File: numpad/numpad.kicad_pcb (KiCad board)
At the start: 2 copper layers, 81.3 x 121.9 mm, 50 parts, among them J1 USB_mini_micro_B, K1 KEYSW, K10 KEYSW, K11 KEYSW, K12 KEYSW, K13 KEYSW, K14 KEYSW, K15 KEYSW, K16 KEYSW, K17 KEYSW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

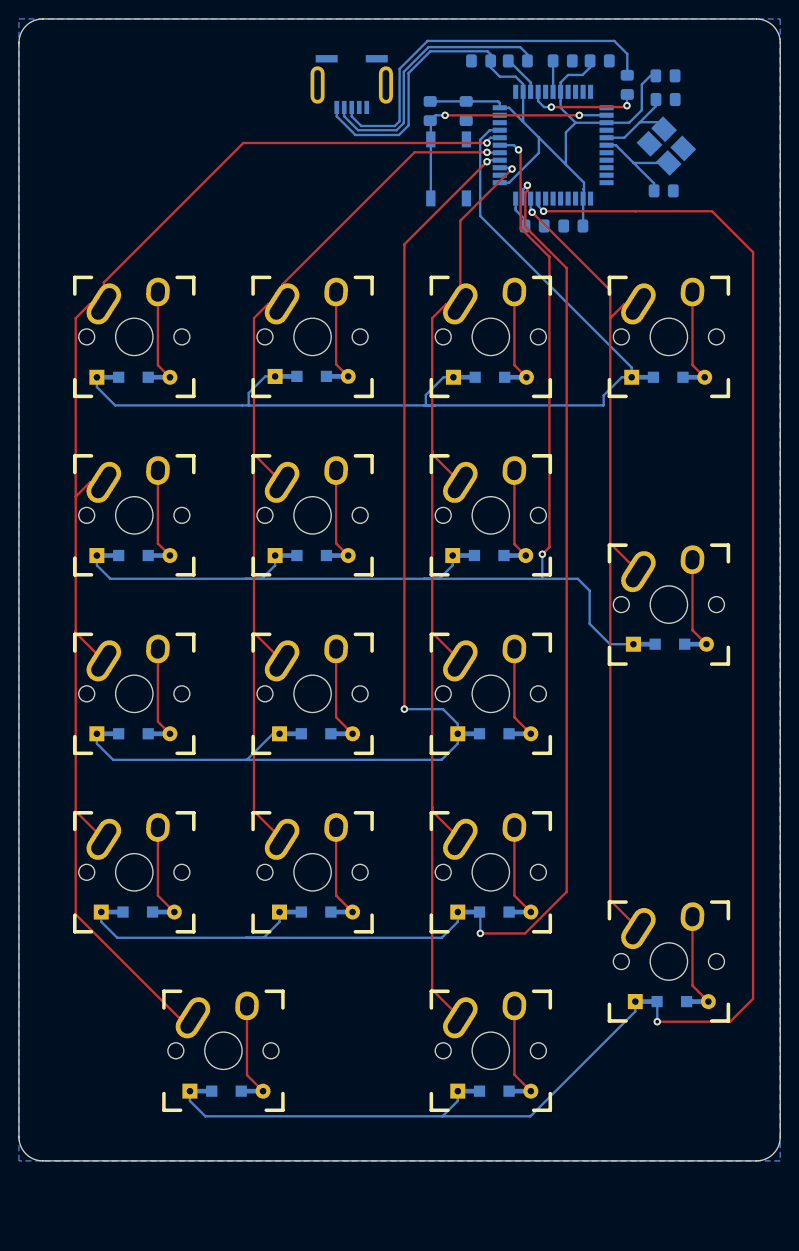
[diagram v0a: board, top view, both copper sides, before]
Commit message: added mounting holes, exported gerber files for manufacturing
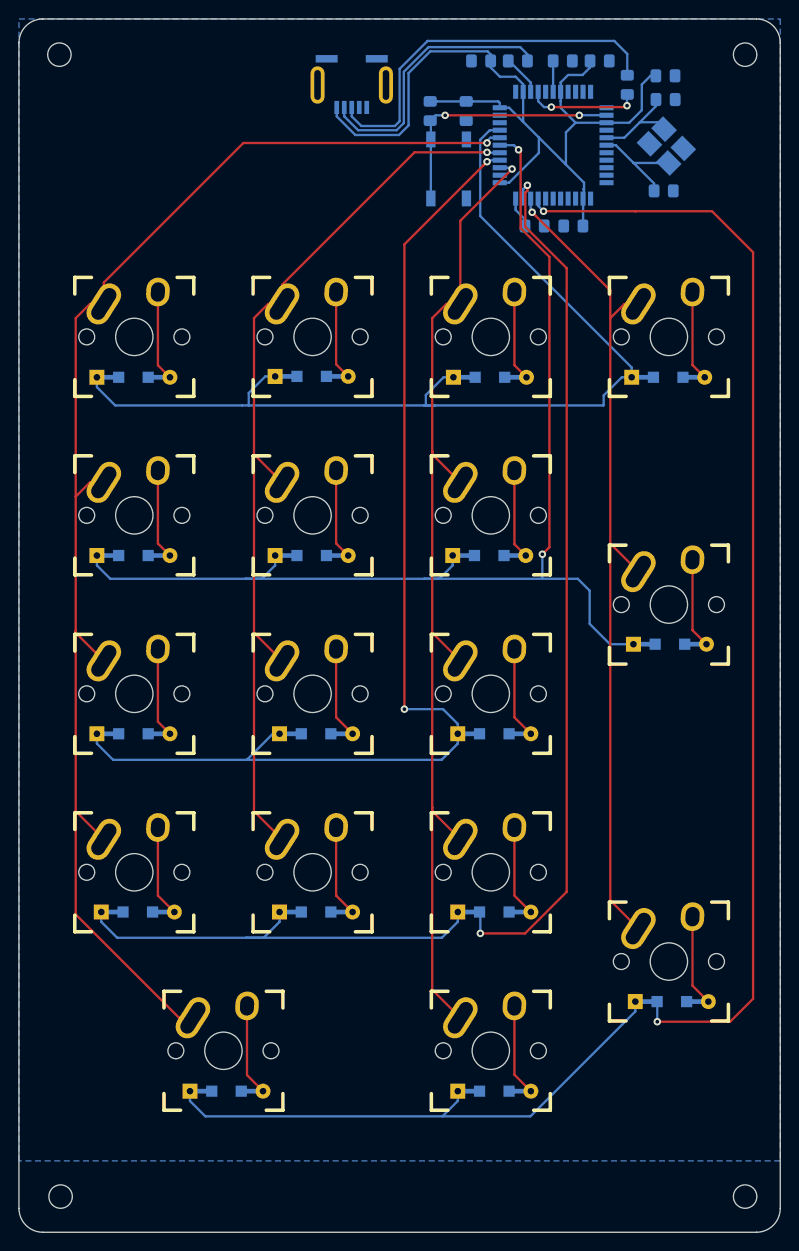
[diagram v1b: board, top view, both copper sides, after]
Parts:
- added REF**: MountingHole_2.5mm, MountingHole:MountingHole_2.5mm, F.Cu at (176.6, 151.1)
- added REF**: MountingHole_2.5mm, MountingHole:MountingHole_2.5mm, F.Cu at (103.5, 151.1)
- added REF**: MountingHole_2.5mm, MountingHole:MountingHole_2.5mm, F.Cu at (176.6, 29.2)
- added REF**: MountingHole_2.5mm, MountingHole:MountingHole_2.5mm, F.Cu at (103.4, 29.2)
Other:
- board size 81.3 x 121.9 mm -> 81.3 x 129.5 mm
- board text added: "Patrick Chau Numpad v1.0"
